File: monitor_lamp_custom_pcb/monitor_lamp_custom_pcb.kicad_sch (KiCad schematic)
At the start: 24 parts, among them IC1 HUSB238, J1 USB_C_Receptacle_PowerOnly_6P, Q1 AO3401A, U1 TPS563300, U2 TPS561208DDCT

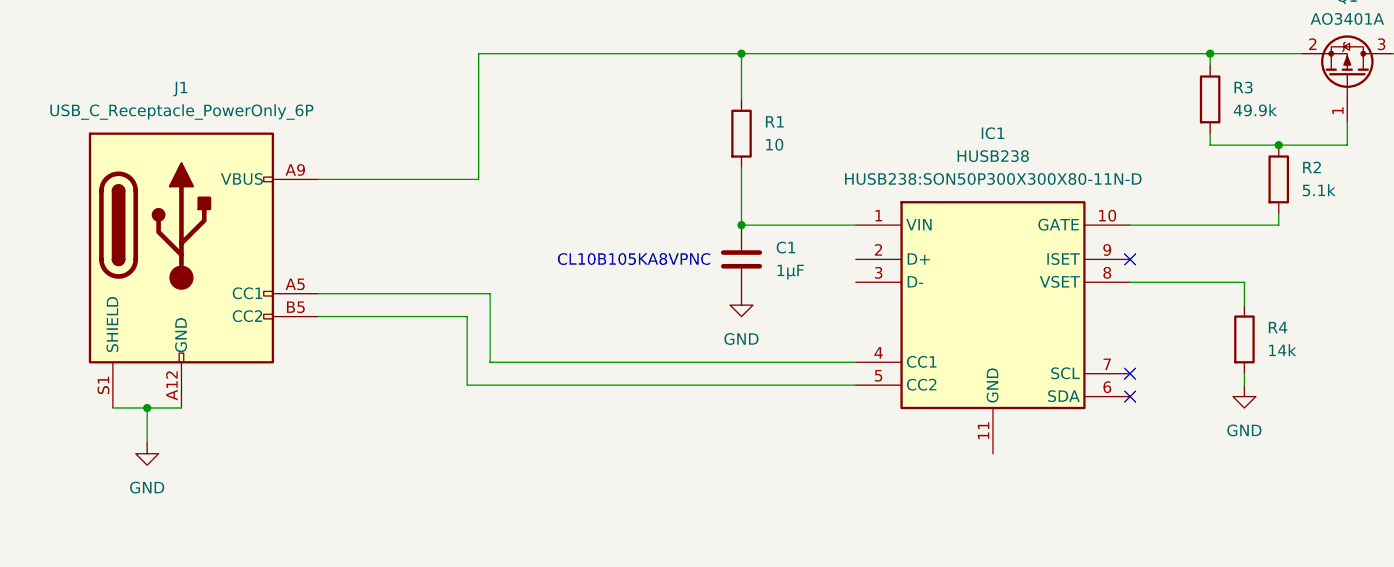
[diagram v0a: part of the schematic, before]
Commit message: Added custom library component to the project
In Kicad not all components are present in the default library, some sensors or modules have to be manually added importing symbols and footprint.
Putting this components inside the project is useful so if someone will download it, in is not necessary to search and import the components
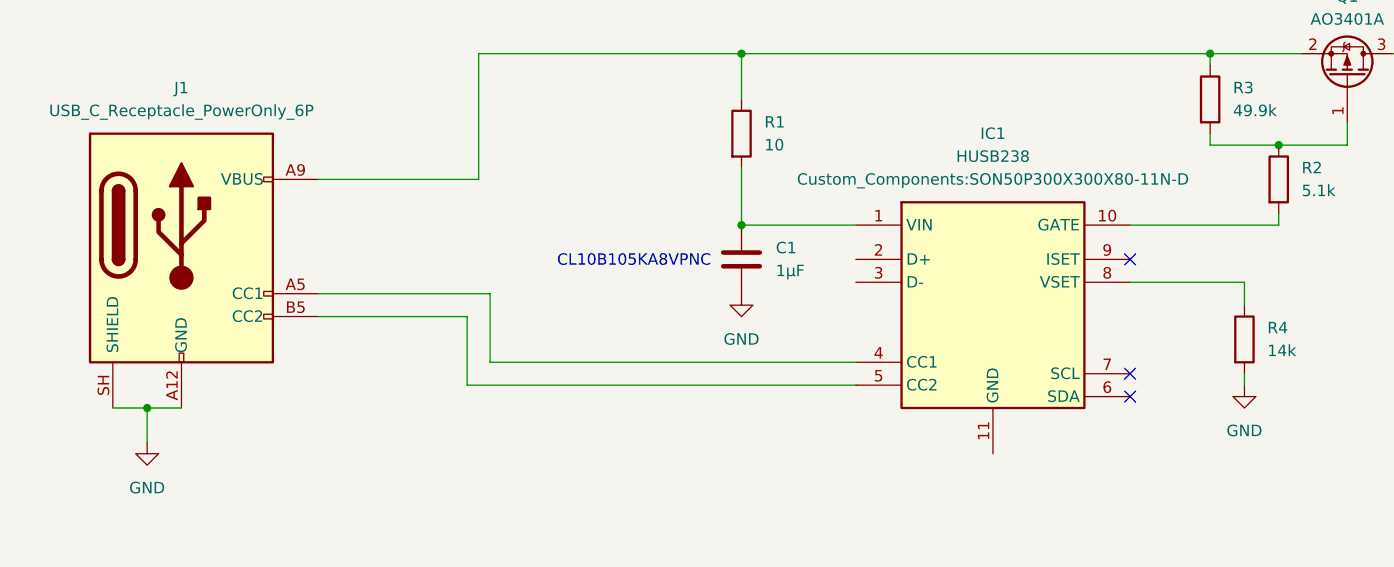
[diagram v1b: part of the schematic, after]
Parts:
- IC1: footprint HUSB238:SON50P300X300X80-11N-D -> Custom_Components:SON50P300X300X80-11N-D
- J1: footprint Connector_USB:USB_C_Receptacle_GCT_USB4125-xx-x-0190_6P_TopMnt_Horizontal -> (none)
- U2: footprint custom:SOT95P280X110-6N -> Custom_Components:SOT95P280X110-6N
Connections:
- net GND: now also J1.SH (SHIELD); no longer J1.S1 (SHIELD)

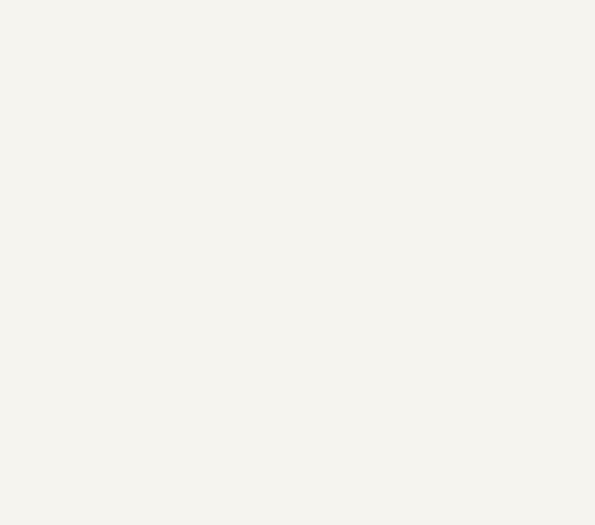
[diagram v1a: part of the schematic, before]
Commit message: Started to place component in the pcb design.
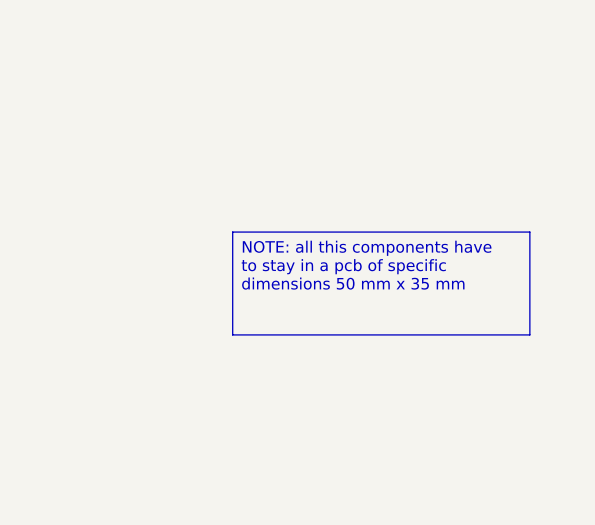
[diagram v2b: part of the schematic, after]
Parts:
- J1: footprint (none) -> Connector_USB:USB_C_Receptacle_GCT_USB4125-xx-x_6P_TopMnt_Horizontal
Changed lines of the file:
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@@
+		)
+	)
+	(text_box "NOTE: all this components have to stay in a pcb of specific dimensions 50 mm x 35 mm"
+		(exclude_from_sim yes)
+		(at 247.65 151.13 0)
+		(size 33.02 11.43)
+		(margins 0.9525 0.9525 0.9525 0.9525)
+		(stroke
+			(width 0)
+			(type solid)
+		)
+		(fill
+			(type none)
+		)
+		(effects
+			(font
+				(size 1.27 1.27)
+				(thickness 0.1588)
+			)
+			(justify left top)
 		)
 	)
@@
 			)
 		)
-		(property "Footprint" ""
+		(property "Footprint" "Connector_USB:USB_C_Receptacle_GCT_USB4125-xx-x_6P_TopMnt_Horizontal"
 			(at 36.83 43.18 0)
 			(hide yes)

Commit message: Started to place components on the board layout
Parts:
- R4: footprint Resistor_SMD:R_0603_1608Metric -> Resistor_SMD:R_0402_1005Metric
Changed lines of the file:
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@@
 			)
 		)
-		(property "Footprint" "Resistor_SMD:R_0603_1608Metric"
+		(property "Footprint" "Resistor_SMD:R_0402_1005Metric"
 			(at 149.352 55.88 90)
 			(hide yes)

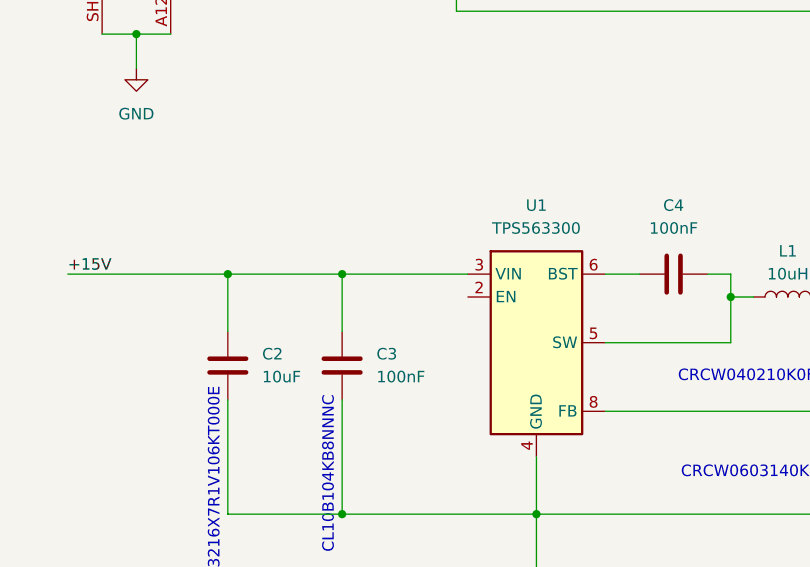
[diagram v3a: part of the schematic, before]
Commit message: Added almost all components to the board. Next step trace
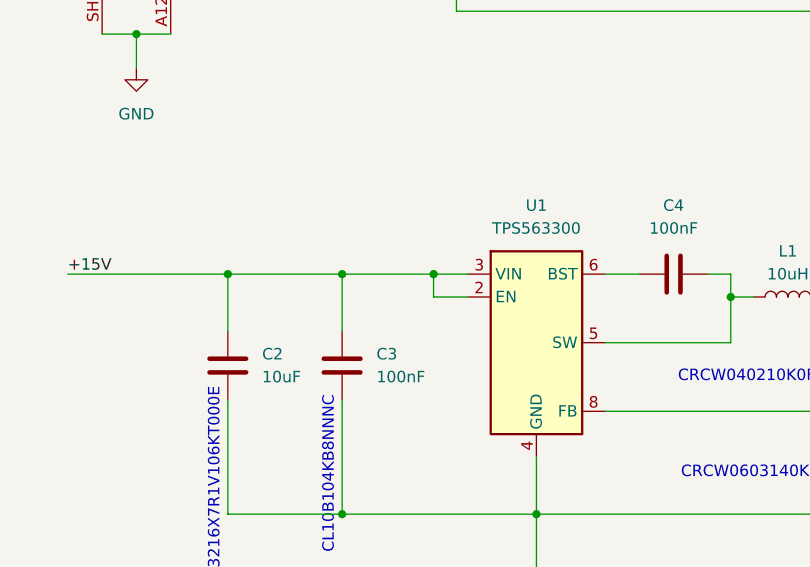
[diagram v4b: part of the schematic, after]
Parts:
- C2: footprint Capacitor_SMD:C_1206_3216Metric -> Capacitor_SMD:C_0805_2012Metric
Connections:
- net +15V: now also U1.2 (EN)
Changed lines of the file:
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@@
+		(color 0 0 0 0)
+	)
+	(junction
+		(at 62.23 90.17)
+		(diameter 0)
 		(color 0 0 0 0)
 	)
@@
 	(wire
 		(pts
+			(xy 62.23 90.17) (xy 66.04 90.17)
+		)
+		(stroke
+			(width 0)
+			(type default)
+		)
+	)
+	(wire
+		(pts
 			(xy 52.07 104.14) (xy 52.07 116.84)
 		)
@@
 	(wire
 		(pts
+			(xy 66.04 92.71) (xy 62.23 92.71)
+		)
+		(stroke
+			(width 0)
+			(type default)
+		)
+	)
+	(wire
+		(pts
 			(xy 59.69 148.59) (xy 59.69 151.13)
 		)
@@
 	(wire
 		(pts
+			(xy 62.23 92.71) (xy 62.23 90.17)
+		)
+		(stroke
+			(width 0)
+			(type default)
+		)
+	)
+	(wire
+		(pts
 			(xy 110.49 102.87) (xy 110.49 105.41)
 		)
@@
 	(wire
 		(pts
-			(xy 52.07 90.17) (xy 66.04 90.17)
+			(xy 52.07 90.17) (xy 62.23 90.17)
 		)
 		(stroke
@@
 			)
 		)
-		(property "Footprint" "Capacitor_SMD:C_1206_3216Metric"
+		(property "Footprint" "Capacitor_SMD:C_0805_2012Metric"
 			(at 40.3352 104.14 0)
 			(hide yes)

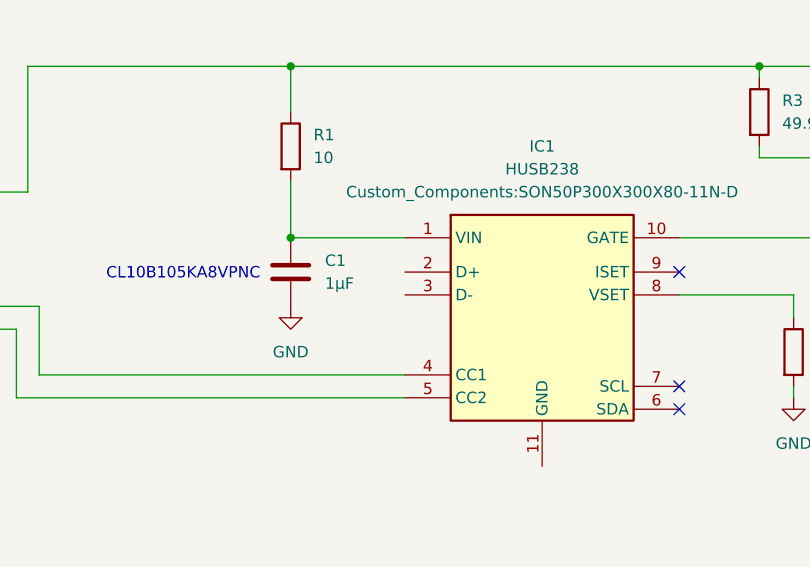
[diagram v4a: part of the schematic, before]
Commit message: Modified layout and J2&J3 connectors
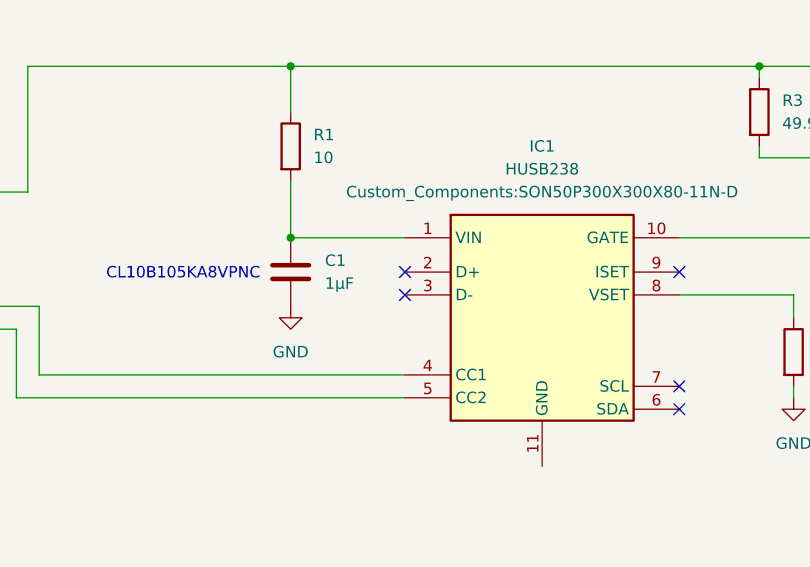
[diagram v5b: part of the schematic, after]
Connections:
- no-connect marks 3 -> 5
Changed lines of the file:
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@@
+	)
+	(no_connect
+		(at 107.95 49.53)
 	)
 	(no_connect
@@
 		(at 138.43 46.99)
 	)
+	(no_connect
+		(at 107.95 46.99)
+	)
 	(wire

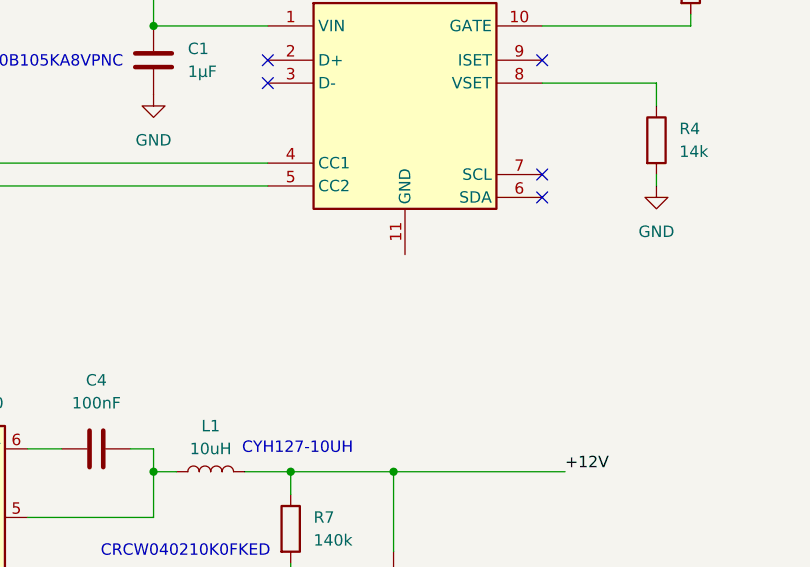
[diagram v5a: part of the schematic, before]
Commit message: Selected 4-Layer setup. Started to trace
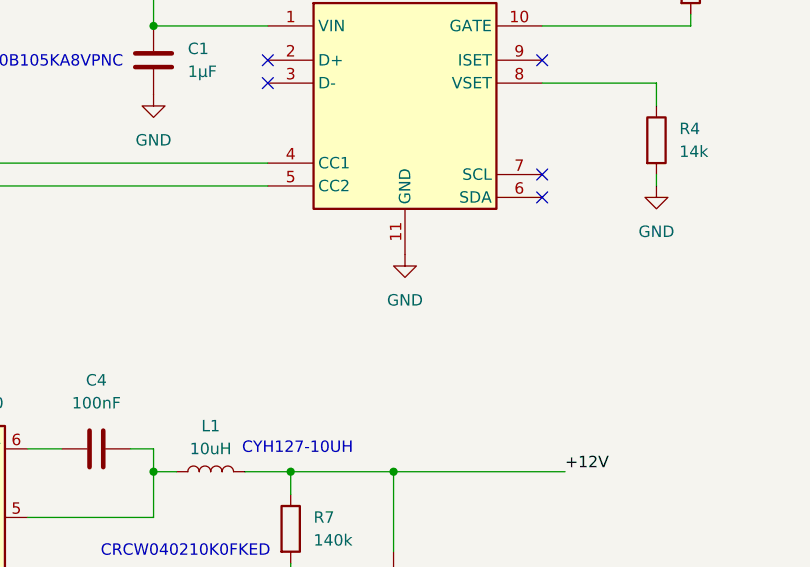
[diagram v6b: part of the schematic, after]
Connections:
- net GND: now also IC1.11 (GND)
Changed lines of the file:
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@@
+	)
+	(symbol
+		(lib_id "power:GND")
+		(at 123.19 68.58 0)
+		(unit 1)
+		(body_style 1)
+		(exclude_from_sim no)
+		(in_bom yes)
+		(on_board yes)
+		(in_pos_files yes)
+		(dnp no)
+		(fields_autoplaced yes)
+		(property "Reference" "#PWR06"
+			(at 123.19 74.93 0)
+			(hide yes)
+			(show_name no)
+			(do_not_autoplace no)
+			(effects
+				(font
+					(size 1.27 1.27)
+				)
+			)
+		)
+		(property "Value" "GND"
+			(at 123.19 73.66 0)
+			(show_name no)
+			(do_not_autoplace no)
+			(effects
+				(font
+					(size 1.27 1.27)
+				)
+			)
+		)
+		(property "Footprint" ""
+			(at 123.19 68.58 0)
+			(hide yes)
+			(show_name no)
+			(do_not_autoplace no)
+			(effects
+				(font
+					(size 1.27 1.27)
+				)
+			)
+		)
+		(property "Datasheet" ""
+			(at 123.19 68.58 0)
+			(hide yes)
+			(show_name no)
+			(do_not_autoplace no)
+			(effects
+				(font
+					(size 1.27 1.27)
+				)
+			)
+		)
+		(property "Description" "Power symbol creates a global label with name \"GND\" , ground"
+			(at 123.19 68.58 0)
+			(hide yes)
+			(show_name no)
+			(do_not_autoplace no)
+			(effects
+				(font
+					(size 1.27 1.27)
+				)
+			)
+		)
+		(pin "1"
+		)
+		(instances
+			(project "monitor_lamp_custom_pcb"
+				(path "/77ed2f8f-6c9e-49d8-b473-d071fcc9ba2f"
+					(reference "#PWR06")
+					(unit 1)
+				)
+			)
+		)
 	)
 	(symbol

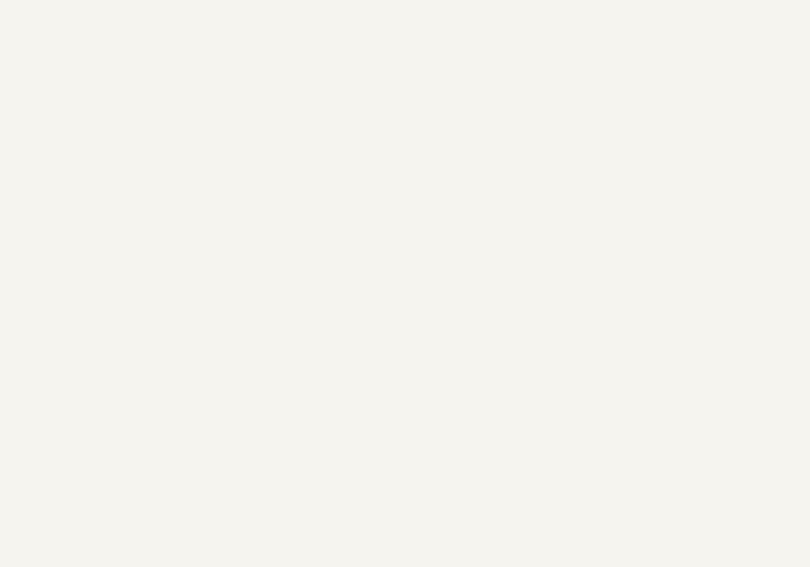
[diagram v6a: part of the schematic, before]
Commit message: Added supplementary power supply connection
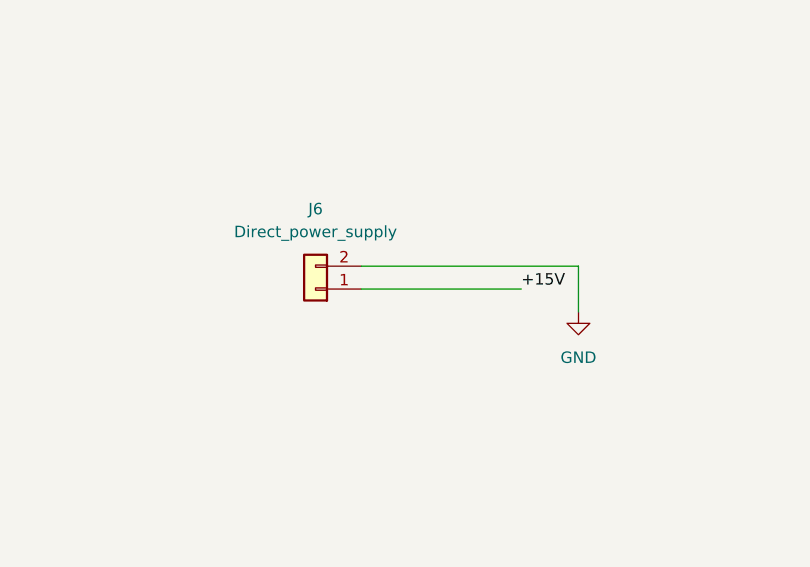
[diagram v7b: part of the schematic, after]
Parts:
- added J6: Direct_power_supply, TerminalBlock:TerminalBlock_Xinya_XY308-2.54-2P_1x02_P2.54mm_Horizontal, symbol Connector_Generic:Conn_01x02
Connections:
- net +15V: now also J6.1 (Pin_1)
- net GND: now also J6.2 (Pin_2)
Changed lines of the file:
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@@
+	(wire
+		(pts
+			(xy 189.23 101.6) (xy 213.36 101.6)
+		)
+		(stroke
+			(width 0)
+			(type default)
+		)
+	)
 	(wire
 		(pts
@@
 	(wire
 		(pts
+			(xy 213.36 101.6) (xy 213.36 106.68)
+		)
+		(stroke
+			(width 0)
+			(type default)
+		)
+	)
+	(wire
+		(pts
 			(xy 138.43 43.18) (xy 154.94 43.18)
 		)
@@
 		(pts
 			(xy 62.23 92.71) (xy 62.23 90.17)
+		)
+		(stroke
+			(width 0)
+			(type default)
+		)
+	)
+	(wire
+		(pts
+			(xy 189.23 104.14) (xy 207.01 104.14)
 		)
 		(stroke
@@
 	(label "+12V"
 		(at 226.06 41.91 0)
+		(effects
+			(font
+				(size 1.27 1.27)
+			)
+			(justify left bottom)
+		)
+	)
+	(label "+15V"
+		(at 207.01 104.14 0)
 		(effects
 			(font
@@
 	)
 	(symbol
+		(lib_id "Connector_Generic:Conn_01x02")
+		(at 184.15 104.14 180)
+		(unit 1)
+		(body_style 1)
+		(exclude_from_sim no)
+		(in_bom yes)
+		(on_board yes)
+		(in_pos_files yes)
+		(dnp no)
+		(fields_autoplaced yes)
+		(property "Reference" "J6"
+			(at 184.15 95.25 0)
+			(show_name no)
+			(do_not_autoplace no)
+			(effects
+				(font
+					(size 1.27 1.27)
+				)
+			)
+		)
+		(property "Value" "Direct_power_supply"
+			(at 184.15 97.79 0)
+			(show_name no)
+			(do_not_autoplace no)
+			(effects
+				(font
+					(size 1.27 1.27)
+				)
+			)
+		)
+		(property "Footprint" "TerminalBlock:TerminalBlock_Xinya_XY308-2.54-2P_1x02_P2.54mm_Horizontal"
+			(at 184.15 104.14 0)
+			(hide yes)
+			(show_name no)
+			(do_not_autoplace no)
+			(effects
+				(font
+					(size 1.27 1.27)
+				)
+			)
+		)
+		(property "Datasheet" ""
+			(at 184.15 104.14 0)
+			(hide yes)
+			(show_name no)
+			(do_not_autoplace no)
+			(effects
+				(font
+					(size 1.27 1.27)
+				)
+			)
+		)
+		(property "Description" "Generic connector, single row, 01x02, script generated (kicad-library-utils/schlib/autogen/connector/)"
+			(at 184.15 104.14 0)
+			(hide yes)
+			(show_name no)
+			(do_not_autoplace no)
+			(effects
+				(font
+					(size 1.27 1.27)
+				)
+			)
+		)
+		(pin "1"
+		)
+		(pin "2"
+		)
+		(instances
+			(project "monitor_lamp_custom_pcb"
+				(path "/77ed2f8f-6c9e-49d8-b473-d071fcc9ba2f"
+					(reference "J6")
+					(unit 1)
+				)
+			)
+		)
+	)
+	(symbol
 		(lib_id "Device:C")
 		(at 40.64 160.02 0)
@@
 					(unit 1)
 				)
+			)
+		)
+	)
+	(symbol
+		(lib_id "power:GND")
+		(at 213.36 106.68 0)
+		(unit 1)
+		(body_style 1)
+		(exclude_from_sim no)
+		(in_bom yes)
+		(on_board yes)
+		(in_pos_files yes)
+		(dnp no)
+		(fields_autoplaced yes)
+		(property "Reference" "#PWR07"
+			(at 213.36 113.03 0)
+			(hide yes)
+			(show_name no)
+			(do_not_autoplace no)
+			(effects
+				(font
+					(size 1.27 1.27)
+				)
+			)
+		)
+		(property "Value" "GND"
+			(at 213.36 111.76 0)
+			(show_name no)
+			(do_not_autoplace no)
+			(effects
+				(font
+					(size 1.27 1.27)
+				)
+			)
+		)
+		(property "Footprint" ""
+			(at 213.36 106.68 0)
+			(hide yes)
+			(show_name no)
+			(do_not_autoplace no)
+			(effects
+				(font
+					(size 1.27 1.27)
+				)
+			)
+		)
+		(property "Datasheet" ""
+			(at 213.36 106.68 0)
+			(hide yes)
+			(show_name no)
+			(do_not_autoplace no)
+			(effects
+				(font
+					(size 1.27 1.27)
+				)
+			)
+		)
+		(property "Description" "Power symbol creates a global label with name \"GND\" , ground"
+			(at 213.36 106.68 0)
+			(hide yes)
+			(show_name no)
+			(do_not_autoplace no)
+			(effects
+				(font
+					(size 1.27 1.27)
+				)
+			)
+		)
+		(pin "1"
+		)
+		(instances
+			(project "monitor_lamp_custom_pcb"
+				(path "/77ed2f8f-6c9e-49d8-b473-d071fcc9ba2f"
+					(reference "#PWR07")
+					(unit 1)
+				)

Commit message: Changed all resistors footprint to R_0603_1608 metric
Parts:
- R10, R2, R3, R4, R7, R9: footprint Resistor_SMD:R_0402_1005Metric -> Resistor_SMD:R_0603_1608Metric
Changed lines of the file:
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@@
 			)
 		)
-		(property "Footprint" "Resistor_SMD:R_0402_1005Metric"
+		(property "Footprint" "Resistor_SMD:R_0603_1608Metric"
 			(at 112.522 165.1 90)
 			(hide yes)
@@
 			)
 		)
-		(property "Footprint" "Resistor_SMD:R_0402_1005Metric"
+		(property "Footprint" "Resistor_SMD:R_0603_1608Metric"
 			(at 145.542 29.21 90)
 			(hide yes)
@@
 			)
 		)
-		(property "Footprint" "Resistor_SMD:R_0402_1005Metric"
+		(property "Footprint" "Resistor_SMD:R_0603_1608Metric"
 			(at 153.162 38.1 90)
 			(hide yes)
@@
 			)
 		)
-		(property "Footprint" "Resistor_SMD:R_0402_1005Metric"
+		(property "Footprint" "Resistor_SMD:R_0603_1608Metric"
 			(at 108.712 99.06 90)
 			(hide yes)
@@
 			)
 		)
-		(property "Footprint" "Resistor_SMD:R_0402_1005Metric"
+		(property "Footprint" "Resistor_SMD:R_0603_1608Metric"
 			(at 149.352 55.88 90)
 			(hide yes)
@@
 			)
 		)
-		(property "Footprint" "Resistor_SMD:R_0402_1005Metric"
+		(property "Footprint" "Resistor_SMD:R_0603_1608Metric"
 			(at 112.522 153.67 90)
 			(hide yes)
